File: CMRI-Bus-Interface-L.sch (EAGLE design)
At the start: 19 parts, among them CON1 0.100, CON2 0.100, U1 MAX3465CPD

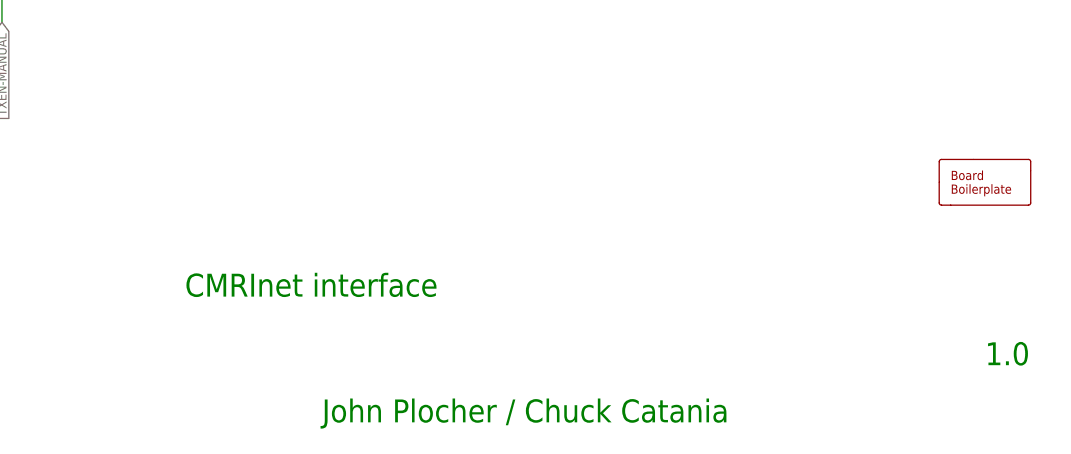
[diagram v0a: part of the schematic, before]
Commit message: v1.1 - changed BOARD to be a 10cmx10cm size so that V-Scores allowed
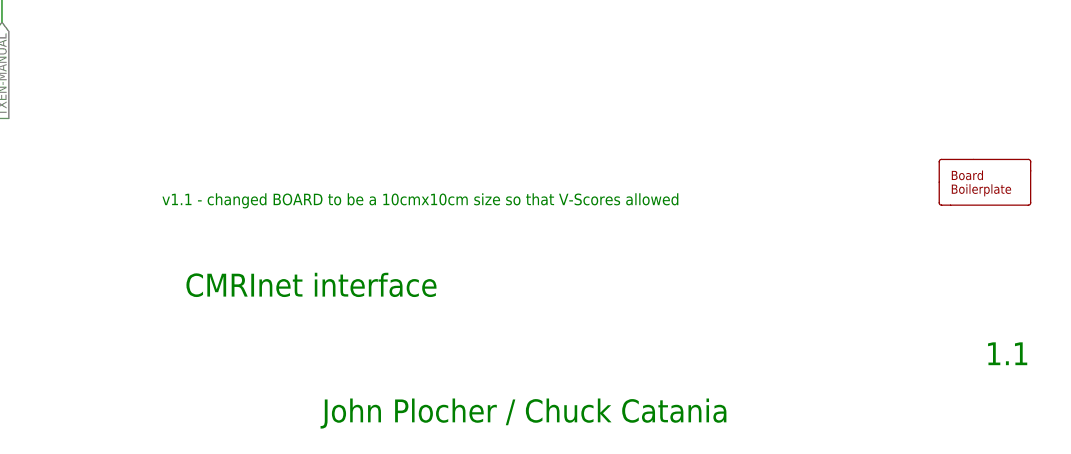
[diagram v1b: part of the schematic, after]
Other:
- note added: "1.1"
- note added: "v1.1 - changed BOARD to be a 10cmx10cm size so that V-Scores allowed"
- note removed: "1.0"
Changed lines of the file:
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@@
 <grid distance="100" unitdist="mil" unit="mil" style="dots" multiple="1" display="yes" altdistance="50" altunitdist="mil" altunit="mil"/>
 <layers>
-<layer number="1" name="Top" color="4" fill="1" visible="yes" active="no"/>
-<layer number="2" name="Route2" color="1" fill="3" visible="yes" active="no"/>
-<layer number="3" name="Route3" color="4" fill="3" visible="yes" active="no"/>
-<layer number="14" name="Route14" color="1" fill="6" visible="yes" active="no"/>
-<layer number="15" name="Route15" color="4" fill="6" visible="yes" active="no"/>
-<layer number="16" name="Bottom" color="1" fill="1" visible="yes" active="no"/>
-<layer number="17" name="Pads" color="2" fill="1" visible="yes" active="no"/>
-<layer number="18" name="Vias" color="2" fill="1" visible="yes" active="no"/>
-<layer number="19" name="Unrouted" color="6" fill="1" visible="yes" active="no"/>
-<layer number="20" name="Dimension" color="15" fill="1" visible="yes" active="no"/>
-<layer number="21" name="tPlace" color="7" fill="1" visible="yes" active="no"/>
-<layer number="22" name="bPlace" color="7" fill="1" visible="yes" active="no"/>
-<layer number="23" name="tOrigins" color="15" fill="1" visible="yes" active="no"/>
-<layer number="24" name="bOrigins" color="15" fill="1" visible="yes" active="no"/>
-<layer number="25" name="tNames" color="7" fill="1" visible="yes" active="no"/>
-<layer number="26" name="bNames" color="7" fill="1" visible="yes" active="no"/>
-<layer number="27" name="tValues" color="7" fill="1" visible="yes" active="no"/>
-<layer number="28" name="bValues" color="7" fill="1" visible="yes" active="no"/>
+<layer number="1" name="Top" color="4" fill="1" visible="no" active="no"/>
+<layer number="2" name="Route2" color="1" fill="3" visible="no" active="no"/>
+<layer number="3" name="Route3" color="4" fill="3" visible="no" active="no"/>
+<layer number="14" name="Route14" color="1" fill="6" visible="no" active="no"/>
+<layer number="15" name="Route15" color="4" fill="6" visible="no" active="no"/>
+<layer number="16" name="Bottom" color="1" fill="1" visible="no" active="no"/>
+<layer number="17" name="Pads" color="2" fill="1" visible="no" active="no"/>
+<layer number="18" name="Vias" color="2" fill="1" visible="no" active="no"/>
+<layer number="19" name="Unrouted" color="6" fill="1" visible="no" active="no"/>
+<layer number="20" name="Dimension" color="15" fill="1" visible="no" active="no"/>
+<layer number="21" name="tPlace" color="7" fill="1" visible="no" active="no"/>
+<layer number="22" name="bPlace" color="7" fill="1" visible="no" active="no"/>
+<layer number="23" name="tOrigins" color="15" fill="1" visible="no" active="no"/>
+<layer number="24" name="bOrigins" color="15" fill="1" visible="no" active="no"/>
+<layer number="25" name="tNames" color="7" fill="1" visible="no" active="no"/>
+<layer number="26" name="bNames" color="7" fill="1" visible="no" active="no"/>
+<layer number="27" name="tValues" color="7" fill="1" visible="no" active="no"/>
+<layer number="28" name="bValues" color="7" fill="1" visible="no" active="no"/>
 <layer number="29" name="tStop" color="7" fill="3" visible="no" active="no"/>
 <layer number="30" name="bStop" color="7" fill="6" visible="no" active="no"/>
@@
 <layer number="35" name="tGlue" color="7" fill="4" visible="no" active="no"/>
 <layer number="36" name="bGlue" color="7" fill="5" visible="no" active="no"/>
-<layer number="37" name="tTest" color="7" fill="1" visible="yes" active="no"/>
-<layer number="38" name="bTest" color="7" fill="1" visible="yes" active="no"/>
+<layer number="37" name="tTest" color="7" fill="1" visible="no" active="no"/>
+<layer number="38" name="bTest" color="7" fill="1" visible="no" active="no"/>
 <layer number="39" name="tKeepout" color="4" fill="11" visible="no" active="no"/>
 <layer number="40" name="bKeepout" color="1" fill="11" visible="no" active="no"/>
@@
 <layer number="44" name="Drills" color="7" fill="1" visible="no" active="no"/>
 <layer number="45" name="Holes" color="7" fill="1" visible="no" active="no"/>
-<layer number="46" name="Milling" color="3" fill="1" visible="yes" active="no"/>
-<layer number="47" name="Measures" color="7" fill="1" visible="yes" active="no"/>
-<layer number="48" name="Document" color="7" fill="1" visible="yes" active="no"/>
-<layer number="49" name="Reference" color="7" fill="1" visible="yes" active="no"/>
-<layer number="50" name="dxf" color="7" fill="1" visible="yes" active="no"/>
-<layer number="51" name="tDocu" color="7" fill="1" visible="yes" active="no"/>
-<layer number="52" name="bDocu" color="7" fill="1" visible="yes" active="no"/>
-<layer number="53" name="tGND_GNDA" color="7" fill="9" visible="yes" active="no"/>
-<layer number="54" name="bGND_GNDA" color="1" fill="9" visible="yes" active="no"/>
-<layer number="56" name="wert" color="7" fill="1" visible="yes" active="no"/>
-<layer number="57" name="tCAD" color="7" fill="1" visible="yes" active="no"/>
-<layer number="59" name="tCarbon" color="7" fill="1" visible="yes" active="no"/>
-<layer number="60" name="bCarbon" color="7" fill="1" visible="yes" active="no"/>
+<layer number="46" name="Milling" color="3" fill="1" visible="no" active="no"/>
+<layer number="47" name="Measures" color="7" fill="1" visible="no" active="no"/>
+<layer number="48" name="Document" color="7" fill="1" visible="no" active="no"/>
+<layer number="49" name="Reference" color="7" fill="1" visible="no" active="no"/>
+<layer number="50" name="dxf" color="7" fill="1" visible="no" active="no"/>
+<layer number="51" name="tDocu" color="7" fill="1" visible="no" active="no"/>
+<layer number="52" name="bDocu" color="7" fill="1" visible="no" active="no"/>
+<layer number="53" name="tGND_GNDA" color="7" fill="9" visible="no" active="no"/>
+<layer number="54" name="bGND_GNDA" color="1" fill="9" visible="no" active="no"/>
+<layer number="56" name="wert" color="7" fill="1" visible="no" active="no"/>
+<layer number="57" name="tCAD" color="7" fill="1" visible="no" active="no"/>
+<layer number="59" name="tCarbon" color="7" fill="1" visible="no" active="no"/>
+<layer number="60" name="bCarbon" color="7" fill="1" visible="no" active="no"/>
 <layer number="90" name="Modules" color="5" fill="1" visible="yes" active="yes"/>
 <layer number="91" name="Nets" color="2" fill="1" visible="yes" active="yes"/>
@@
 <layer number="255" name="routoute" color="7" fill="1" visible="yes" active="yes"/>
 </layers>
-<schematic xreflabel="%F%N/%S.%C%R" xrefpart="/%S.%C%R">
+<schematic xreflabel="%F%N" xrefpart="/%S.%C%R">
 <attributes>
 </attributes>
@@
 <wire x1="104.14" y1="7.62" x2="104.14" y2="139.7" width="0.000153125" layer="97"/>
 <wire x1="104.14" y1="139.7" x2="5.08" y2="139.7" width="0.000153125" layer="97"/>
-<text x="238.76" y="12.7" size="2.54" layer="91">1.0</text>
+<text x="238.76" y="12.7" size="2.54" layer="91">1.1</text>
 <text x="149.86" y="20.32" size="2.54" layer="91">CMRInet interface</text>
 <text x="165.1" y="6.35" size="2.54" layer="91">John Plocher / Chuck Catania</text>
@@
 <wire x1="15.24" y1="27.94" x2="22.86" y2="27.94" width="0.000153125" layer="98"/>
 <wire x1="22.86" y1="27.94" x2="22.86" y2="71.12" width="0.000153125" layer="98"/>
+<text x="147.32" y="30.48" size="1.27" layer="91">v1.1 - changed BOARD to be a 10cmx10cm size so that V-Scores allowed</text>
 </plain>
 <instances>

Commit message: added missing component values
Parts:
- CMRI-IO: value (none) -> 0.100
- CMRINET3, CMRINET4: value Molex -> 0.156
- U2: value (none) -> NE555
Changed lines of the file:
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@@
 <layer number="255" name="routoute" color="7" fill="1" visible="yes" active="yes"/>
 </layers>
-<schematic xreflabel="%F%N" xrefpart="/%S.%C%R">
+<schematic xreflabel="%F%N/%S.%C%R" xrefpart="/%S.%C%R">
 <attributes>
 </attributes>
@@
 </classes>
 <parts>
-<part name="U2" library="SPCoast" deviceset="NE555" device="P"/>
+<part name="U2" library="SPCoast" deviceset="NE555" device="P" value="NE555"/>
 <part name="U1" library="SPCoast" deviceset="MAX346*" device="PD" technology="5C"/>
 <part name="C1" library="SPCoast" deviceset="CAP*" device="PTH1" value="0.1uF"/>
@@
 <part name="GND9" library="SparkFun" deviceset="GND" device=""/>
 <part name="CMRINET2" library="SPCoast" deviceset="CONNECTOR-CMRINET" device="3.5MM" value="3.5mm"/>
-<part name="CMRINET3" library="SPCoast" deviceset="CONNECTOR-CMRINET" device=".156" value="Molex"/>
-<part name="CMRINET4" library="SPCoast" deviceset="CONNECTOR-CMRINET" device=".156" value="Molex"/>
+<part name="CMRINET3" library="SPCoast" deviceset="CONNECTOR-CMRINET" device=".156" value="0.156"/>
+<part name="CMRINET4" library="SPCoast" deviceset="CONNECTOR-CMRINET" device=".156" value="0.156"/>
 <part name="TX" library="SPCoast" deviceset="LED*" device="LED5MM"/>
 <part name="BOARD1" library="SPCoast" deviceset="BOARD" device="80X60" value="BOARD80X60"/>
 <part name="CMRINET1" library="SPCoast" deviceset="CONNECTOR-CMRINET" device="3.5MM" value="3.5mm"/>
-<part name="CMRI-IO" library="SPCoast" deviceset="CONNECTOR-M05" device="CMRI"/>
+<part name="CMRI-IO" library="SPCoast" deviceset="CONNECTOR-M05" device="CMRI" value="0.100"/>
 <part name="GND2" library="SparkFun" deviceset="GND" device=""/>
 <part name="P+3" library="SparkFun" deviceset="VCC" device=""/>
@@
 <attribute name="VALUE" x="217.17" y="95.25" size="1.778" layer="96" rot="MR180"/>
 </instance>
-<instance part="CMRI-IO" gate="G$1" x="121.92" y="81.28"/>
+<instance part="CMRI-IO" gate="CON1" x="121.92" y="81.28"/>
 <instance part="GND2" gate="1" x="144.78" y="73.66"/>
 <instance part="P+3" gate="1" x="149.86" y="78.74"/>
@@
 <instance part="GND4" gate="1" x="25.4" y="22.86"/>
 <instance part="J1" gate="J" x="127" y="55.88" rot="R90"/>
-<instance part="CON1" gate="G$1" x="238.76" y="144.78" smashed="yes" rot="R180">
+<instance part="CON1" gate="CON1" x="238.76" y="144.78" smashed="yes" rot="R180">
 <attribute name="VALUE" x="242.57" y="135.89" size="1.778" layer="96" rot="R180"/>
 </instance>
-<instance part="CON2" gate="G$1" x="241.3" y="104.14" smashed="yes" rot="R180">
+<instance part="CON2" gate="CON1" x="241.3" y="104.14" smashed="yes" rot="R180">
 <attribute name="VALUE" x="245.11" y="95.25" size="1.778" layer="96" rot="R180"/>
 </instance>
@@
 </segment>
 <segment>
-<pinref part="CMRI-IO" gate="G$1" pin="2"/>
+<pinref part="CMRI-IO" gate="CON1" pin="2"/>
 <wire x1="129.54" y1="78.74" x2="149.86" y2="78.74" width="0.1524" layer="91"/>
 <pinref part="P+3" gate="1" pin="VCC"/>
@@
 </segment>
 <segment>
-<pinref part="CMRI-IO" gate="G$1" pin="1"/>
+<pinref part="CMRI-IO" gate="CON1" pin="1"/>
 <wire x1="129.54" y1="76.2" x2="144.78" y2="76.2" width="0.1524" layer="91"/>
 <pinref part="GND2" gate="1" pin="GND"/>
@@
 </segment>
 <segment>
-<pinref part="CMRI-IO" gate="G$1" pin="3"/>
+<pinref part="CMRI-IO" gate="CON1" pin="3"/>
 <wire x1="129.54" y1="81.28" x2="134.62" y2="81.28" width="0.1524" layer="91"/>
 <label x="134.62" y="81.28" size="1.27" layer="95" xref="yes"/>
@@
 </segment>
 <segment>
-<pinref part="CMRI-IO" gate="G$1" pin="4"/>
+<pinref part="CMRI-IO" gate="CON1" pin="4"/>
 <wire x1="129.54" y1="83.82" x2="134.62" y2="83.82" width="0.1524" layer="91"/>
 <label x="134.62" y="83.82" size="1.27" layer="95" xref="yes"/>
@@
 <wire x1="210.82" y1="142.24" x2="220.98" y2="142.24" width="0.1524" layer="91"/>
 <junction x="210.82" y="142.24"/>
-<pinref part="CON1" gate="G$1" pin="4"/>
+<pinref part="CON1" gate="CON1" pin="4"/>
 <wire x1="220.98" y1="142.24" x2="231.14" y2="142.24" width="0.1524" layer="91"/>
 <junction x="220.98" y="142.24"/>
 <wire x1="213.36" y1="101.6" x2="223.52" y2="101.6" width="0.1524" layer="91"/>
 <junction x="213.36" y="101.6"/>
-<pinref part="CON2" gate="G$1" pin="4"/>
+<pinref part="CON2" gate="CON1" pin="4"/>
 <wire x1="223.52" y1="101.6" x2="233.68" y2="101.6" width="0.1524" layer="91"/>
 <junction x="223.52" y="101.6"/>
@@
 <wire x1="210.82" y1="144.78" x2="220.98" y2="144.78" width="0.1524" layer="91"/>
 <junction x="210.82" y="144.78"/>
-<pinref part="CON1" gate="G$1" pin="3"/>
+<pinref part="CON1" gate="CON1" pin="3"/>
 <wire x1="220.98" y1="144.78" x2="231.14" y2="144.78" width="0.1524" layer="91"/>
 <junction x="220.98" y="144.78"/>
 <wire x1="213.36" y1="104.14" x2="223.52" y2="104.14" width="0.1524" layer="91"/>
 <junction x="213.36" y="104.14"/>
-<pinref part="CON2" gate="G$1" pin="3"/>
+<pinref part="CON2" gate="CON1" pin="3"/>
 <wire x1="223.52" y1="104.14" x2="233.68" y2="104.14" width="0.1524" layer="91"/>
 <junction x="223.52" y="104.14"/>
@@
 <wire x1="210.82" y1="147.32" x2="220.98" y2="147.32" width="0.1524" layer="91"/>
 <junction x="210.82" y="147.32"/>
-<pinref part="CON1" gate="G$1" pin="2"/>
+<pinref part="CON1" gate="CON1" pin="2"/>
 <wire x1="220.98" y1="147.32" x2="231.14" y2="147.32" width="0.1524" layer="91"/>
 <junction x="220.98" y="147.32"/>
 <wire x1="213.36" y1="106.68" x2="223.52" y2="106.68" width="0.1524" layer="91"/>
 <junction x="213.36" y="106.68"/>
-<pinref part="CON2" gate="G$1" pin="2"/>
+<pinref part="CON2" gate="CON1" pin="2"/>
 <wire x1="223.52" y1="106.68" x2="233.68" y2="106.68" width="0.1524" layer="91"/>
 <junction x="223.52" y="106.68"/>
@@
 <wire x1="210.82" y1="149.86" x2="220.98" y2="149.86" width="0.1524" layer="91"/>
 <junction x="210.82" y="149.86"/>
-<pinref part="CON1" gate="G$1" pin="1"/>
+<pinref part="CON1" gate="CON1" pin="1"/>
 <wire x1="220.98" y1="149.86" x2="231.14" y2="149.86" width="0.1524" layer="91"/>
 <junction x="220.98" y="149.86"/>
 <wire x1="213.36" y1="109.22" x2="223.52" y2="109.22" width="0.1524" layer="91"/>
 <junction x="213.36" y="109.22"/>
-<pinref part="CON2" gate="G$1" pin="1"/>
+<pinref part="CON2" gate="CON1" pin="1"/>
 <wire x1="223.52" y1="109.22" x2="233.68" y2="109.22" width="0.1524" layer="91"/>
 <junction x="223.52" y="109.22"/>
@@
 <wire x1="210.82" y1="139.7" x2="220.98" y2="139.7" width="0.1524" layer="91"/>
 <junction x="210.82" y="139.7"/>
-<pinref part="CON1" gate="G$1" pin="5"/>
+<pinref part="CON1" gate="CON1" pin="5"/>
 <wire x1="220.98" y1="139.7" x2="231.14" y2="139.7" width="0.1524" layer="91"/>
 <junction x="220.98" y="139.7"/>
 <wire x1="213.36" y1="99.06" x2="223.52" y2="99.06" width="0.1524" layer="91"/>
 <junction x="213.36" y="99.06"/>
-<pinref part="CON2" gate="G$1" pin="5"/>
+<pinref part="CON2" gate="CON1" pin="5"/>
 <wire x1="223.52" y1="99.06" x2="233.68" y2="99.06" width="0.1524" layer="91"/>
 <junction x="223.52" y="99.06"/>
@@
 <net name="TXEN-MANUAL" class="0">
 <segment>
-<pinref part="CMRI-IO" gate="G$1" pin="5"/>
+<pinref part="CMRI-IO" gate="CON1" pin="5"/>
 <wire x1="129.54" y1="86.36" x2="134.62" y2="86.36" width="0.1524" layer="91"/>
 <label x="134.62" y="86.36" size="1.27" layer="95" xref="yes"/>
